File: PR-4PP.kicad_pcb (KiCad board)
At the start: 2 copper layers, 24 parts, among them SW1 SW_Push, U1 ATmega32U4-AU, Y1 16mHz

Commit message: finish pcb
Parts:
- removed C2: 0.1uF, Capacitor_SMD:C_0805_2012Metric
- removed the C4 at (44.6, 89.7)
- removed the C6 at (53.2, 68.3)
- added C1: 22pF, Capacitor_SMD:C_0805_2012Metric, B.Cu at (52.4, 68.3)
- added C7: 10uF, Capacitor_SMD:C_0805_2012Metric, B.Cu at (38.7, 84.2)
- added c2: 22pF, Capacitor_SMD:C_0805_2012Metric, B.Cu at (43.7, 68.3)
- C5: value 22pF -> 0.1uF
- moved C4 17.8 mm to (40.5, 71.0)
- moved C5 15.9 mm to (57.7, 75.8), turned to 90 degrees
- moved R1 2.10 mm to (37.3, 71.0), turned to 270 degrees
- moved C6 0.99 mm to (53.3, 89.4)
- moved C3 0.88 mm to (38.4, 78.5)
- renumbered C7 to C3, C1 to C4, C3 to C6, R3 to R1, R1 to R3
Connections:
- C5 pad 1: Net-(C5-Pad1) -> +5V
- U1 pad 17: Net-(C5-Pad1) -> Net-(C1-Pad1)
- U1 pad 27: Net-(U1-Pad27) -> ROW0
- U1 pad 28: Net-(U1-Pad28) -> COL1
- U1 pad 29: Net-(U1-Pad29) -> COL0
- U1 pad 30: Net-(U1-Pad30) -> ROW1
- Y1 pad 1: Net-(C5-Pad1) -> Net-(C1-Pad1)
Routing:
- net GND: track 6.60 -> 142.2 mm
- net +5V: track 0.00 -> 102.0 mm, vias 0 -> 5
- net ROW1: track 0.00 -> 52.3 mm
- net COL1: track 0.00 -> 52.0 mm
- net ROW0: track 0.00 -> 47.4 mm
- net COL0: track 0.00 -> 33.3 mm
- net Net-(R1-Pad2): track 0.00 -> 31.5 mm, vias 0 -> 2
- net Net-(U1-Pad16): track 0.00 -> 11.7 mm
- net VCC: track 0.00 -> 9.23 mm
- net Net-(C1-Pad1): track 0.00 -> 7.92 mm
- net Net-(D4-Pad2): track 0.00 -> 6.82 mm
- net Net-(D2-Pad2): track 0.00 -> 6.82 mm
- net Net-(D3-Pad2): track 0.00 -> 6.82 mm
- net Net-(D1-Pad2): track 0.00 -> 6.59 mm
- net Net-(R4-Pad2): track 0.00 -> 4.08 mm
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
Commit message: route & create gerbers
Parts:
- moved F1 1.77 mm to (26.2, 76.2), turned to 180 degrees
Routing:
- net +5V: track 102.0 -> 99.3 mm
- net VCC: track 9.23 -> 11.4 mm
- net ROW1: track 52.3 -> 53.8 mm
- added copper zone on B.Cu, net GND
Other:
- board outline added: 77 x 38.1 mm
- board text added: "PR-4++"

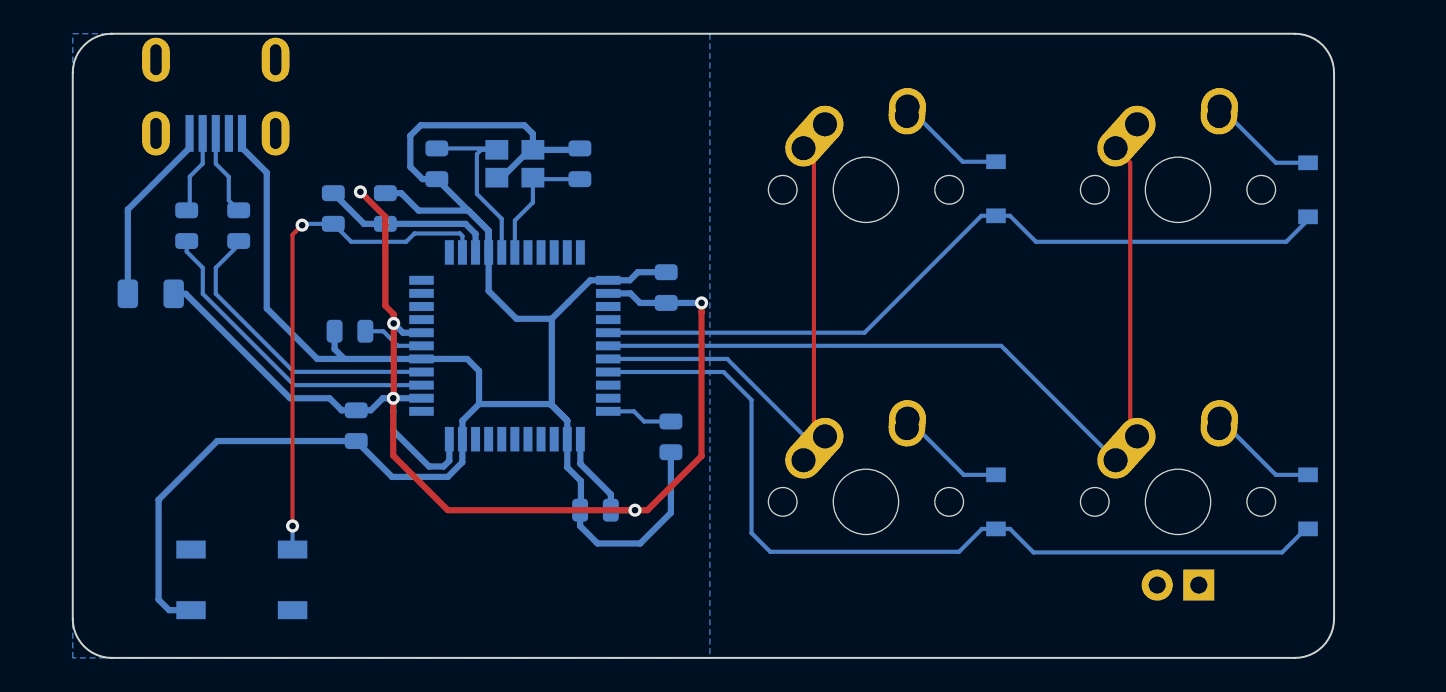
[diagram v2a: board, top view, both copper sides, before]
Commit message: move caps closer
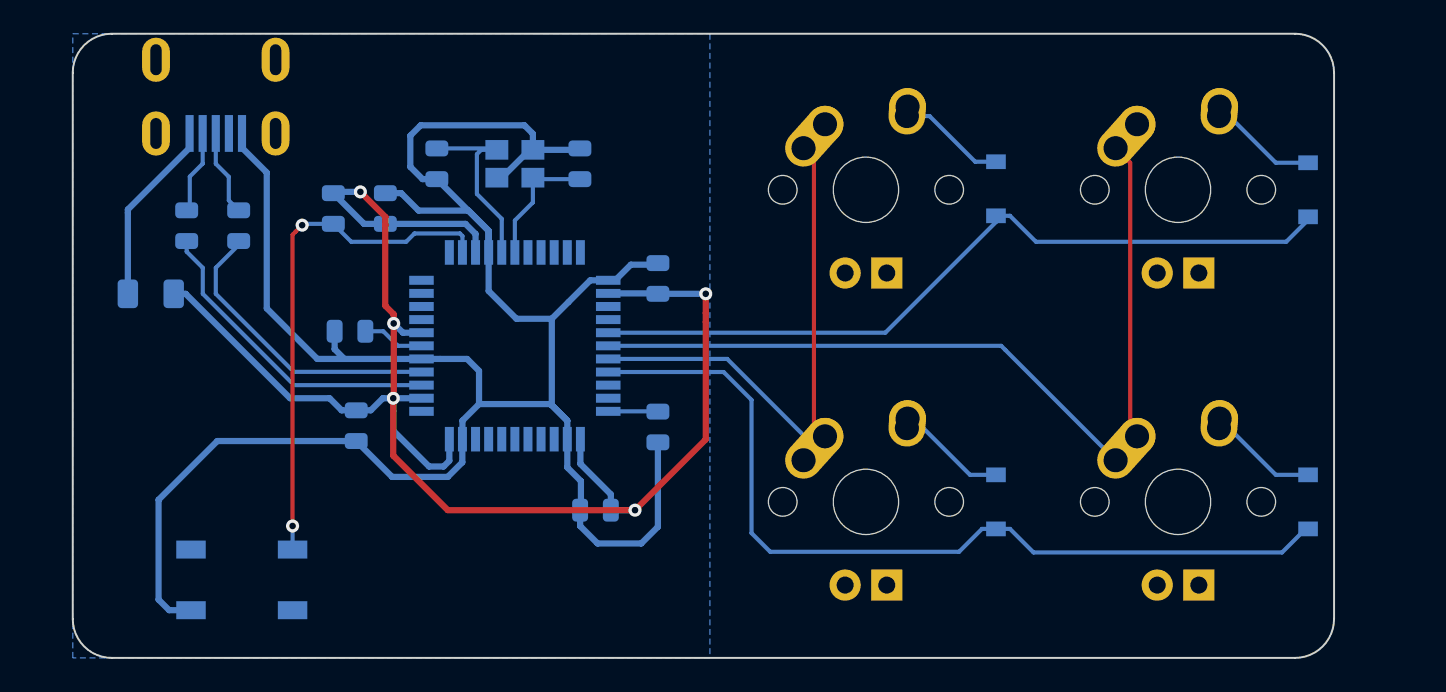
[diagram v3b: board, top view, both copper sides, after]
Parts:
- MX1, MX2, MX3: footprint MX_Alps_Hybrid:MX-1U-NoLED -> MX_Alps_Hybrid:MX-1U
- moved R4 1.00 mm to (57.1, 84.3)
- moved C5 0.75 mm to (57.1, 75.3)
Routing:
- net +5V: track 99.3 -> 101.2 mm
- net Net-(R4-Pad2): track 4.08 -> 3.04 mm
- net GND: track 142.3 -> 141.8 mm

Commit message: reroute usb
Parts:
- added L1: 60@100Mhz, Inductor_SMD:L_1206_3216Metric_Pad1.42x1.75mm_HandSolder, B.Cu at (35.9, 75.9)
- added R5: 5.1k, Capacitor_SMD:C_0805_2012Metric_Pad1.15x1.40mm_HandSolder, B.Cu at (27.0, 71.7)
- added R6: 5.1k, Capacitor_SMD:C_0805_2012Metric_Pad1.15x1.40mm_HandSolder, B.Cu at (32.4, 71.7)
- added U3: SRV05-4, Package_TO_SOT_SMD:SOT-23-6, B.Cu at (29.7, 74.5)
- D1, D2, D3, D4: footprint Diode_SMD:D_SOD-123 -> random-keyboard-parts:D_SOD-123-Pretty
- F1: footprint Fuse:Fuse_1206_3216Metric -> Fuse:Fuse_1206_3216Metric_Pad1.42x1.75mm_HandSolder
- MX1, MX2, MX3: footprint MX_Alps_Hybrid:MX-1U -> MX_Alps_Hybrid:MX-1U-NoLED
- USB1: value Molex-0548190589 -> HRO-TYPE-C-31-M-12; footprint random-keyboard-parts:Molex-0548190589 -> Type-C:HRO-TYPE-C-31-M-12-HandSoldering
- moved SW1 7.98 mm to (39.7, 92.9)
- moved R2 6.11 mm to (30.7, 78.1)
- moved R3 6.05 mm to (28.6, 78.1)
- moved USB1 1.59 mm to (30.2, 60.3), turned to 0 degrees
- moved F1 1.07 mm to (25.1, 76.0), turned to 270 degrees
- renumbered c2 to C2
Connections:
- F1 pad 1: +5V -> VBUS
- F1 pad 2: VCC -> +5V
- USB1 pad 1: GND -> GNDPWR
- USB1 pad 2: Net-(USB1-Pad2) -> VBUS
- USB1 pad 3: D+ -> Net-(USB1-Pad3)
- USB1 pad 4: D- -> Net-(R5-Pad2)
- USB1 pad 5: VCC -> D-
- USB1 pad 6: Net-(USB1-Pad6) -> D+
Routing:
- net GNDPWR: track 0.00 -> 45.6 mm, vias 0 -> 2
- net GND: track 141.8 -> 119.6 mm
- net VBUS: track 0.00 -> 15.7 mm
- net VCC: track 11.4 -> 0.00 mm
- net D-: track 5.10 -> 14.2 mm
- net D+: track 5.27 -> 13.6 mm
- net +5V: track 101.2 -> 108.7 mm
- net Net-(R1-Pad2): track 31.6 -> 38.5 mm
- net Net-(R2-Pad1): track 18.3 -> 13.9 mm
- net Net-(R5-Pad2): track 0.00 -> 3.57 mm
- net Net-(R6-Pad2): track 0.00 -> 3.52 mm
- net Net-(R3-Pad1): track 19.3 -> 16.0 mm
- removed copper zone on B.Cu, net GND

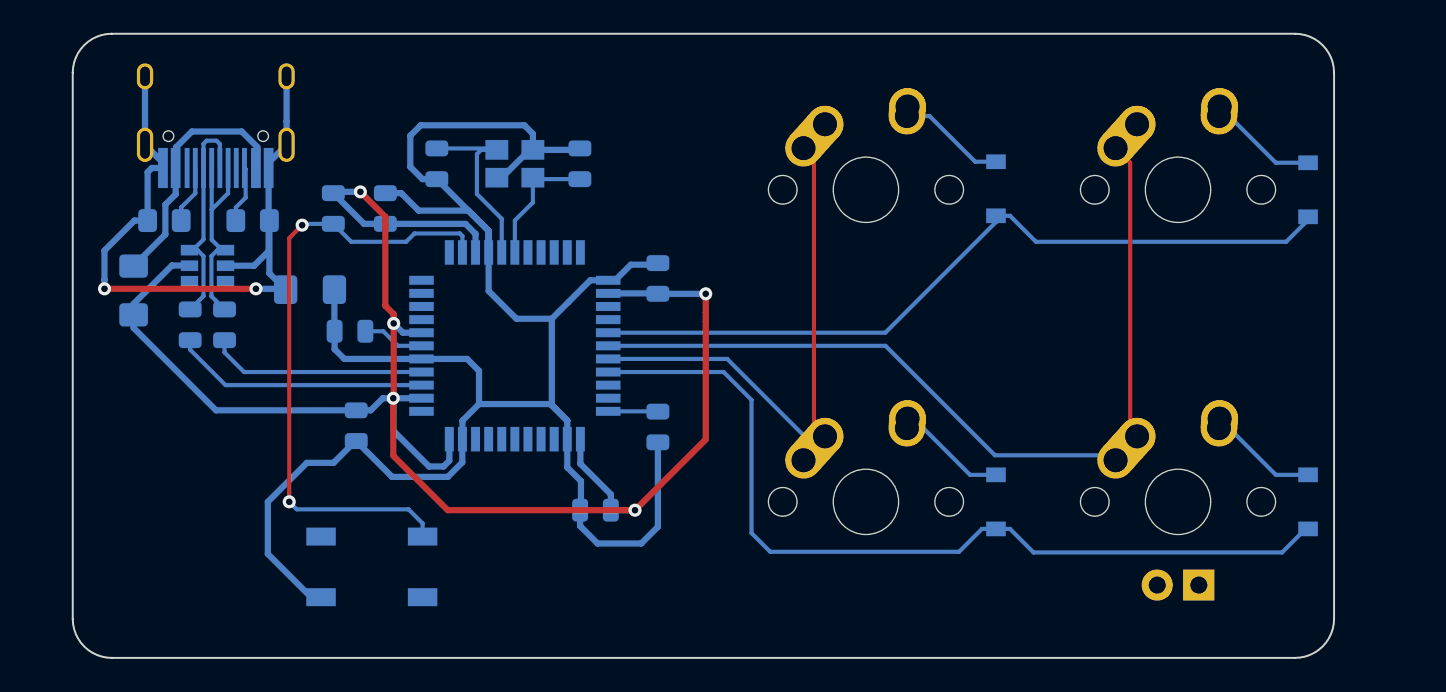
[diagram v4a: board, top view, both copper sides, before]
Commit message: retrace differential data lines
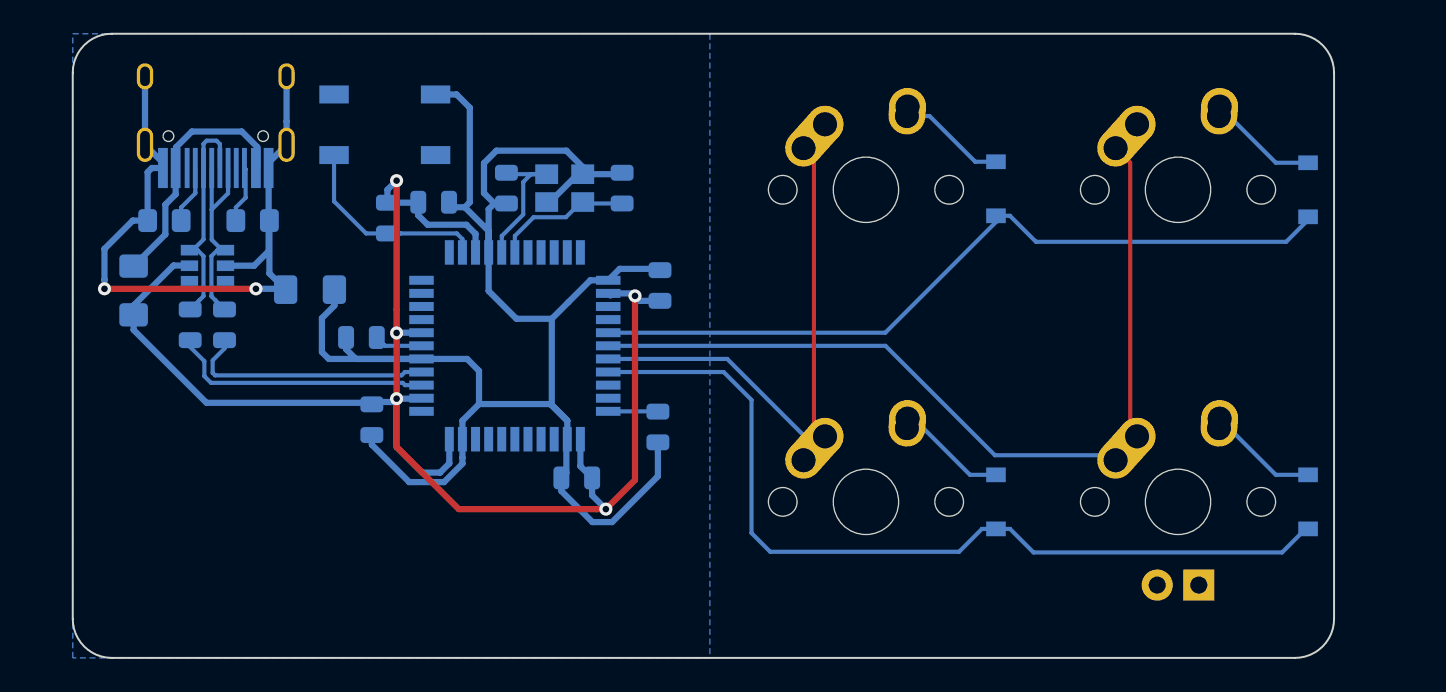
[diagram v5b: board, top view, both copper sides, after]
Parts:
- moved SW1 27.0 mm to (40.5, 65.9), turned to 0 degrees
- moved C2 4.50 mm to (47.9, 69.7)
- moved Y1 3.39 mm to (51.5, 69.7)
- moved R1 3.35 mm to (40.6, 71.6)
- moved C1 2.98 mm to (55.0, 69.7)
- moved C4 2.97 mm to (43.5, 70.6), turned to 0 degrees
- moved C6 2.28 mm to (52.2, 87.4)
- moved C7 1.02 mm to (39.7, 83.9)
- moved C3 0.80 mm to (39.1, 78.9)
- moved C5 0.45 mm to (57.3, 75.7)
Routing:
- net Net-(R1-Pad2): track 38.5 -> 12.4 mm, vias 2 -> 0
- net GND: track 119.6 -> 108.0 mm
- net +5V: track 108.7 -> 99.1 mm
- net Net-(C2-Pad1): track 11.7 -> 8.96 mm
- net Net-(R2-Pad1): track 13.9 -> 15.8 mm
- net Net-(C3-Pad2): track 3.80 -> 2.94 mm
- net Net-(C1-Pad1): track 7.92 -> 8.45 mm
- added copper zone on B.Cu, net GND

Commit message: reroute & fillzones
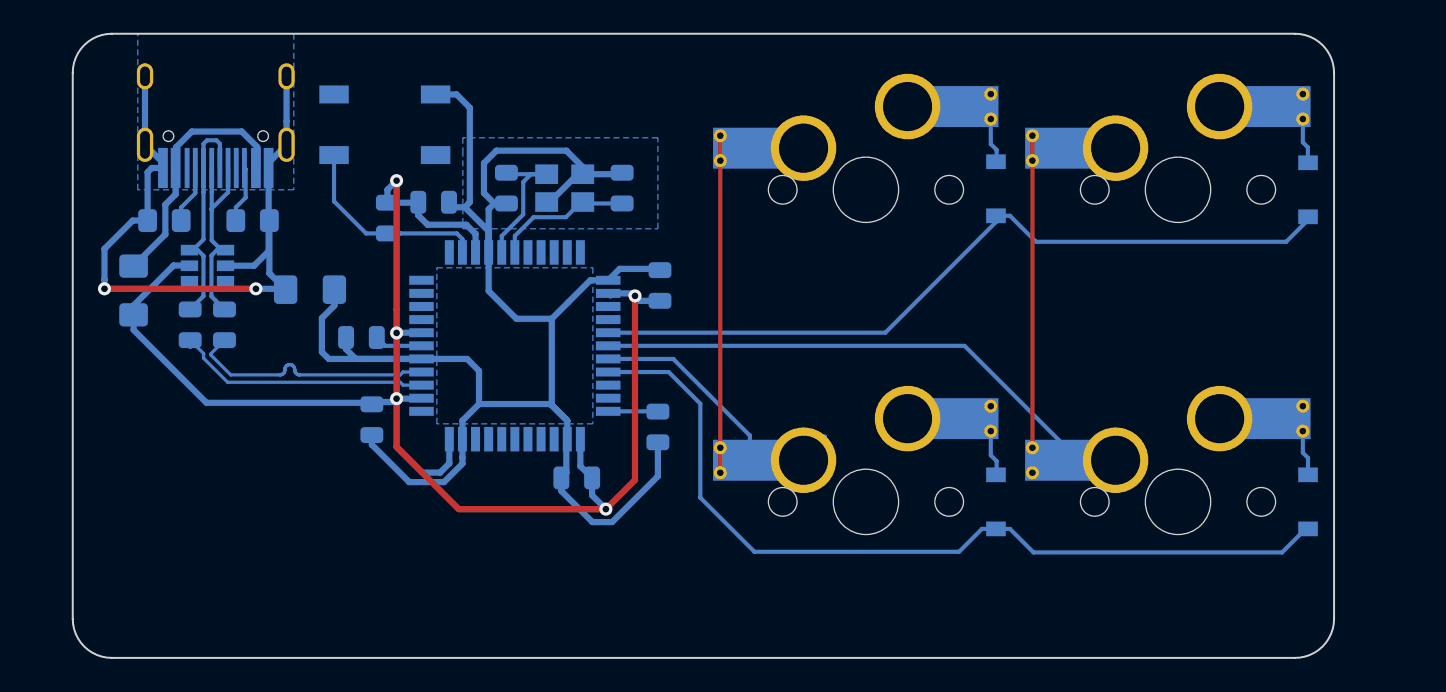
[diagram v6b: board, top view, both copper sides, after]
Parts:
- MX1, MX2, MX3: footprint MX_Alps_Hybrid:MX-1U-NoLED -> MX_Only:MXOnly-1U-Hotswap-Antishear
- MX4: footprint MX_Alps_Hybrid:MX-1U -> MX_Only:MXOnly-1U-Hotswap-Antishear
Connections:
- R2 pad 1: Net-(R2-Pad1) -> D+
- R3 pad 1: Net-(R3-Pad1) -> D-
- U1 pad 3: Net-(R3-Pad1) -> D-
- U1 pad 4: Net-(R2-Pad1) -> D+
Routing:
- net D+: track 13.6 -> 30.0 mm
- net Net-(R3-Pad1): track 16.3 -> 0.00 mm
- net D-: track 14.2 -> 30.3 mm
- net Net-(R2-Pad1): track 15.8 -> 0.00 mm
- net Net-(D4-Pad2): track 6.82 -> 2.80 mm
- net Net-(D2-Pad2): track 6.82 -> 4.32 mm
- net Net-(D1-Pad2): track 6.59 -> 4.15 mm
- net COL0: track 33.3 -> 34.8 mm
- net ROW1: track 53.8 -> 52.4 mm
- net Net-(D3-Pad2): track 6.62 -> 5.36 mm
- added copper zone on B.Cu, net GNDPWR

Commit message: save project
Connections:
- R2 pad 1: D+ -> /DR+
- R3 pad 1: D- -> /DR-
- U1 pad 3: D- -> /DR-
- U1 pad 4: D+ -> /DR+
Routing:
- net D+: track 30.0 -> 13.9 mm
- net /DR+: track 0.00 -> 16.1 mm
- net D-: track 30.3 -> 14.2 mm
- net /DR-: track 0.00 -> 15.7 mm
- net COL1: track 51.9 -> 56.1 mm
- net Net-(D3-Pad2): track 5.36 -> 2.80 mm
- net COL0: track 34.8 -> 32.7 mm
- net Net-(D1-Pad2): track 4.15 -> 2.77 mm
- net VBUS: track 15.7 -> 17.1 mm

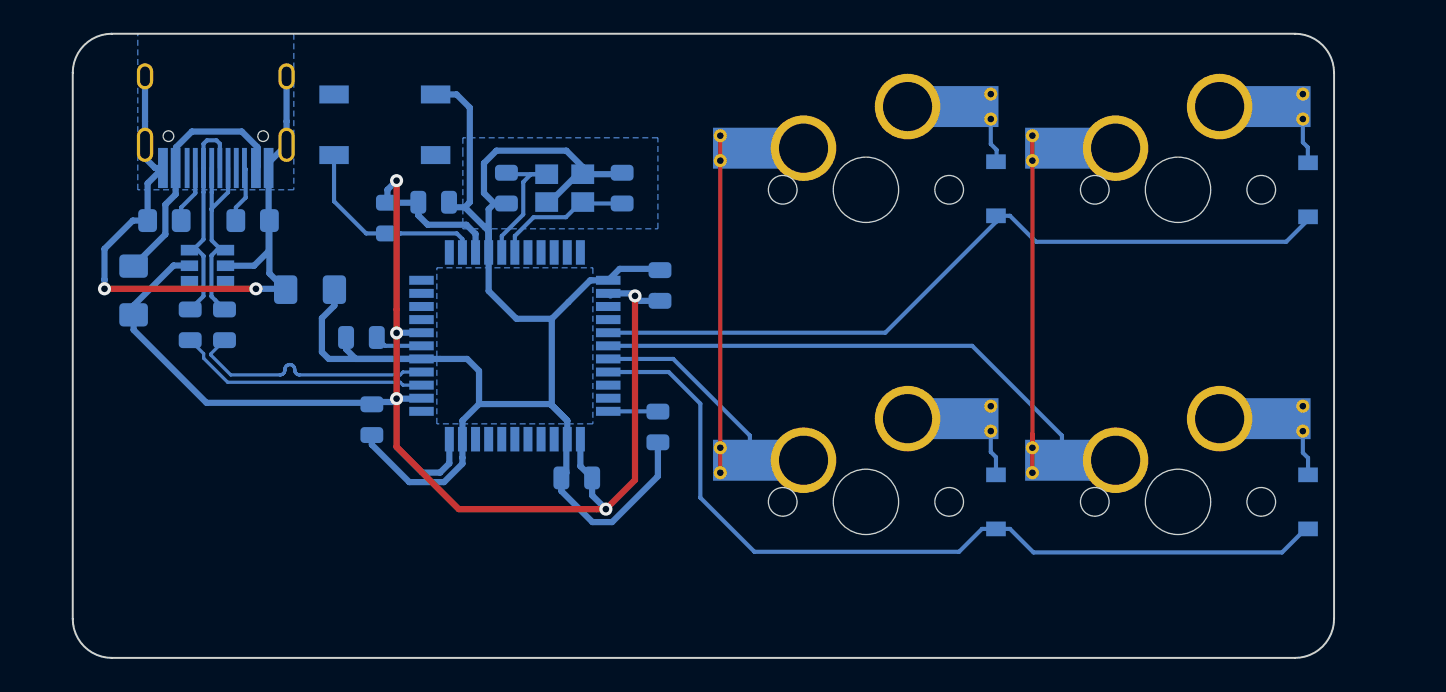
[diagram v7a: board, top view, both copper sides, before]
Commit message: add silkscreen and part numbers
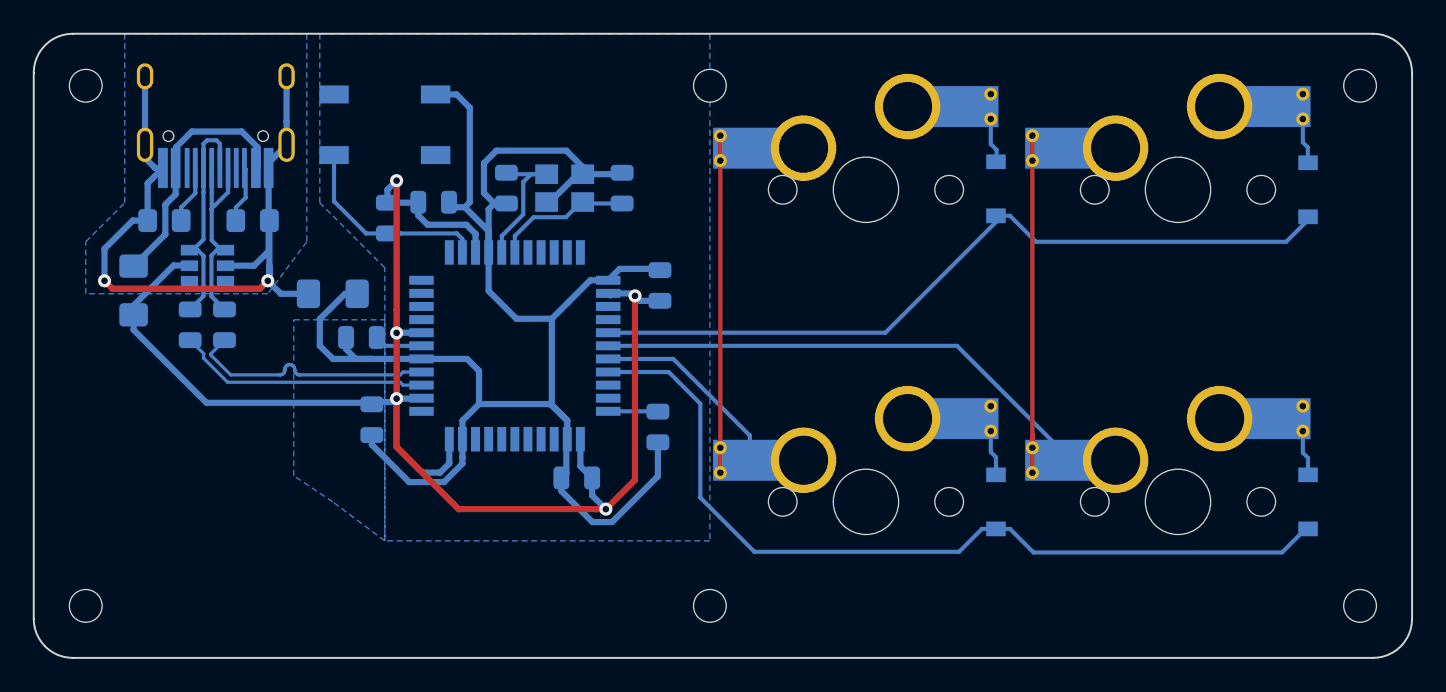
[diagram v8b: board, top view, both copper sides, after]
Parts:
- added Brand: rodpa.dev, PR:rodpadev_logo_40x40mm, B.Cu at (28.6, 88.1)
- added H1: MountingHole, MountingHole:MountingHole_2mm, B.Cu at (22.2, 63.5)
- added H2: MountingHole, MountingHole:MountingHole_2mm, B.Cu at (60.3, 63.5)
- added H3: MountingHole, MountingHole:MountingHole_2mm, B.Cu at (100.0, 63.5)
- added H4: MountingHole, MountingHole:MountingHole_2mm, B.Cu at (22.2, 95.2)
- added H5: MountingHole, MountingHole:MountingHole_2mm, B.Cu at (60.3, 95.2)
- added H6: MountingHole, MountingHole:MountingHole_2mm, B.Cu at (100.0, 95.2)
- added Model: PR-4++, PR:PR-4PP_20x20mm, B.Cu at (50.0, 95.2)
- moved L1 1.41 mm to (37.3, 76.2)
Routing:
- net GND: track 108.0 -> 105.7 mm
- net GNDPWR: track 45.5 -> 46.7 mm
- net COL1: track 56.1 -> 55.6 mm
- added copper zone on B.Cu, net (none)
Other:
- board size 77 x 38.1 mm -> 84.1 x 38.1 mm
- board text removed: "PR-4++"
